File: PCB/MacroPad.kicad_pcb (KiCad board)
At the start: 2 copper layers, 80 x 97.5 mm, 34 parts, among them M1 XIAO-RP2040, SW1 RotaryEncoder_Switch, SW10 SW_Push_45deg, SW11 SW_Push_45deg, SW12 SW_Push_45deg, SW13 SW_Push_45deg, SW14 SW_Push_45deg, SW15 SW_Push_45deg, SW16 SW_Push_45deg, SW17 SW_Push_45deg, SW2 SW_Push_45deg, SW3 SW_Push_45deg, SW4 SW_Push_45deg, SW5 SW_Push_45deg, SW6 SW_Push_45deg, SW7 SW_Push_45deg, SW8 SW_Push_45deg, SW9 SW_Push_45deg

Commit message: Routed and finished PCB
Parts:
- removed M1: XIAO-RP2040, ScottoKeebs_MCU:Seeed_XIAO_RP2040
- added U1: MCU_Seeed_XIAO_RP2040, ScottoKeebs_MCU:Seeed_XIAO_RP2040, B.Cu at (94.0, 77.5)
- D1, D10, D11, D12, D13, D14, D15, D16, D2, D3, D4, D5, D6, D7, D8, D9: footprint Diode_THT:D_DO-35_SOD27_P7.62mm_Horizontal -> ScottoKeebs_Components:Diode_DO-35
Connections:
- SW1 pad S1: unconnected-(SW1-PadS1) -> GND
- SW1 pad S2: unconnected-(SW1-PadS2) -> Net-(U1-PA6_A10_D10_MOSI)
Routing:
- net Row 3: track 0.00 -> 189.3 mm
- net Row 2: track 0.00 -> 141.4 mm, vias 0 -> 3
- net Row 1: track 0.00 -> 120.1 mm
- net Row 0: track 0.00 -> 111.6 mm
- net Col 0: track 0.00 -> 106.7 mm
- net Col 3: track 0.00 -> 97.7 mm
- net Col 1: track 0.00 -> 87.9 mm, vias 0 -> 2
- net Col 2: track 0.00 -> 82.7 mm, vias 0 -> 2
- net GND: track 0.00 -> 82.1 mm
- net Net-(U1-PA6_A10_D10_MOSI): track 0.00 -> 51.5 mm
- net Net-(U1-PA7_A8_D8_SCK): track 0.00 -> 39.4 mm
- net Net-(U1-PB09_A7_D7_RX): track 0.00 -> 32.2 mm
- net Net-(D13-A): track 0.00 -> 7.47 mm
- net Net-(D5-A): track 0.00 -> 7.45 mm
- net Net-(D9-A): track 0.00 -> 7.44 mm
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
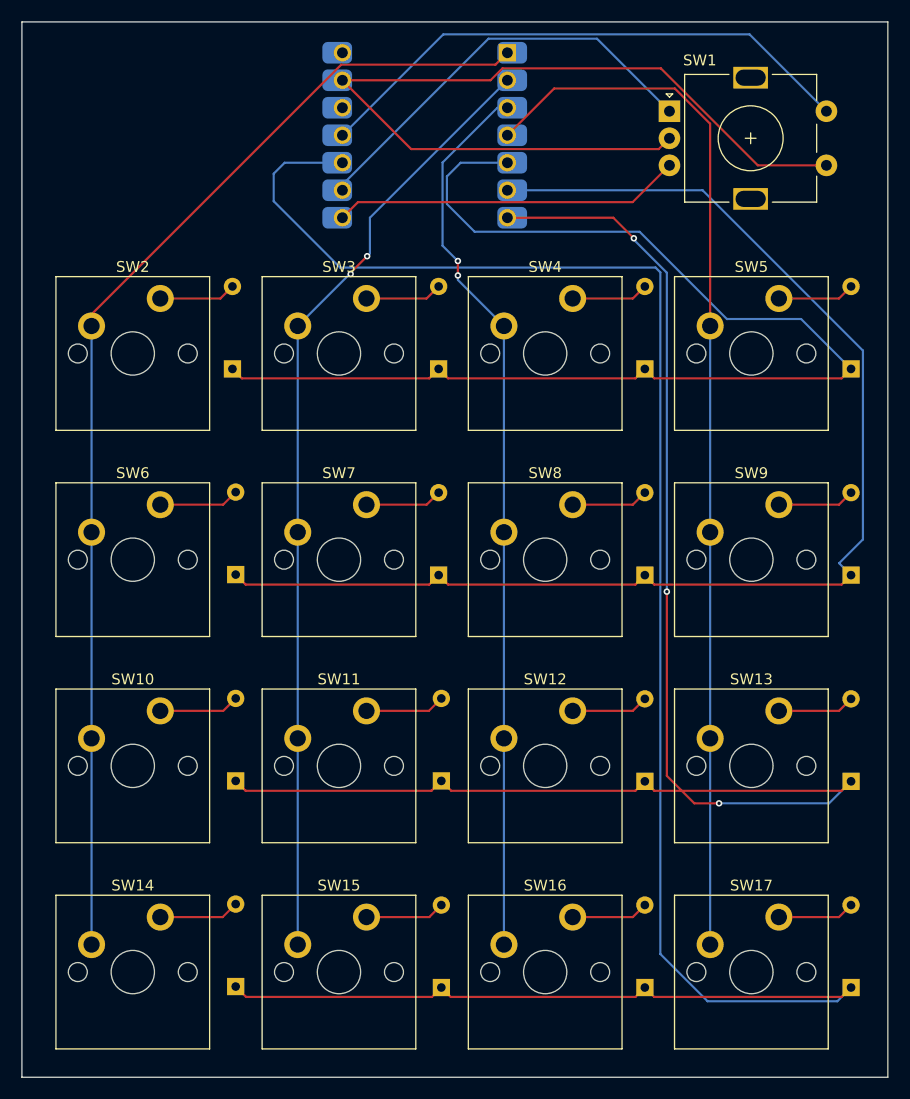
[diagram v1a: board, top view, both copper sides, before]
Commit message: Finished the case and firmware
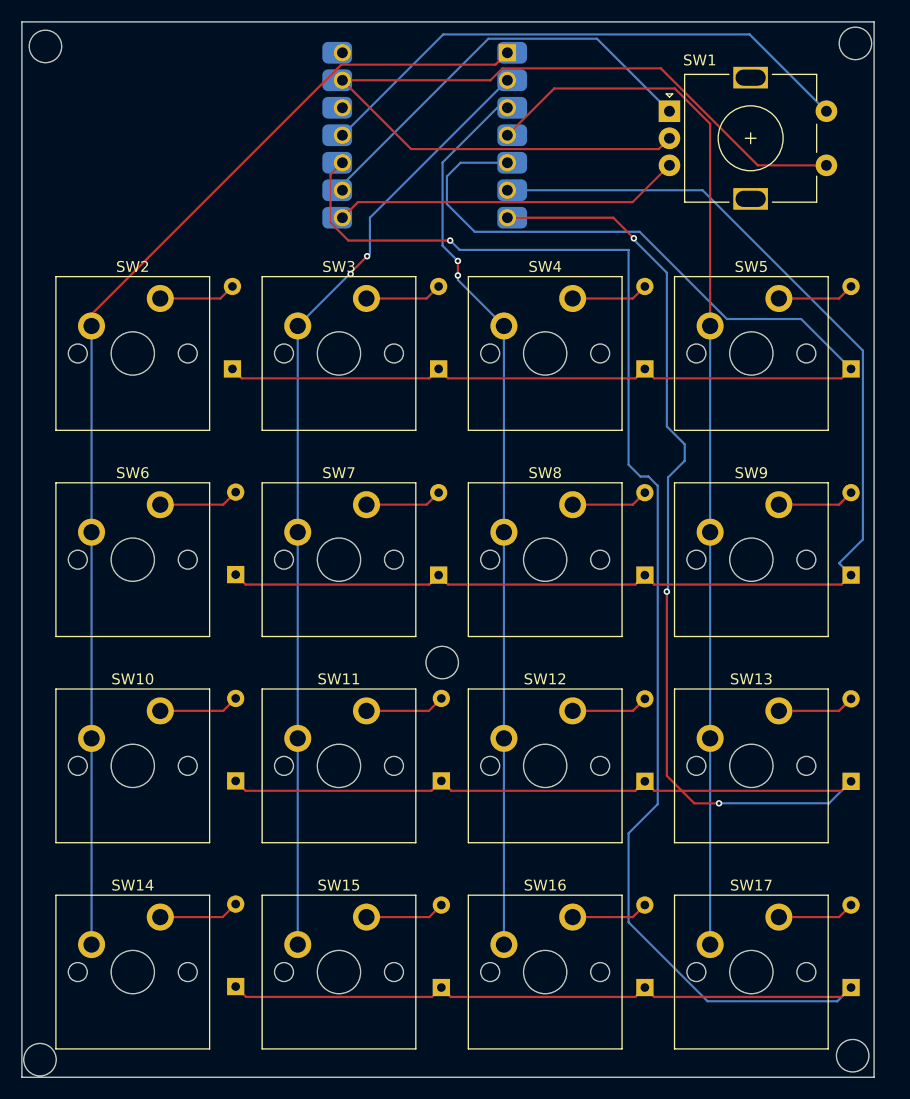
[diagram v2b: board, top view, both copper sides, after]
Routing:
- net Row 3: track 189.3 -> 182.5 mm, vias 0 -> 1
- net Row 2: track 141.4 -> 142.7 mm
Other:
- board size 80 x 97.5 mm -> 78.7 x 97.5 mm
